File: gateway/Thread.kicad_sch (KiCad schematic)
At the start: 27 parts, among them IC1004 MIC5317-3.3xM5, IC1501 TXB0104RUT, M1501 BT40, Q1501 BSS123, X1501 DEBUG

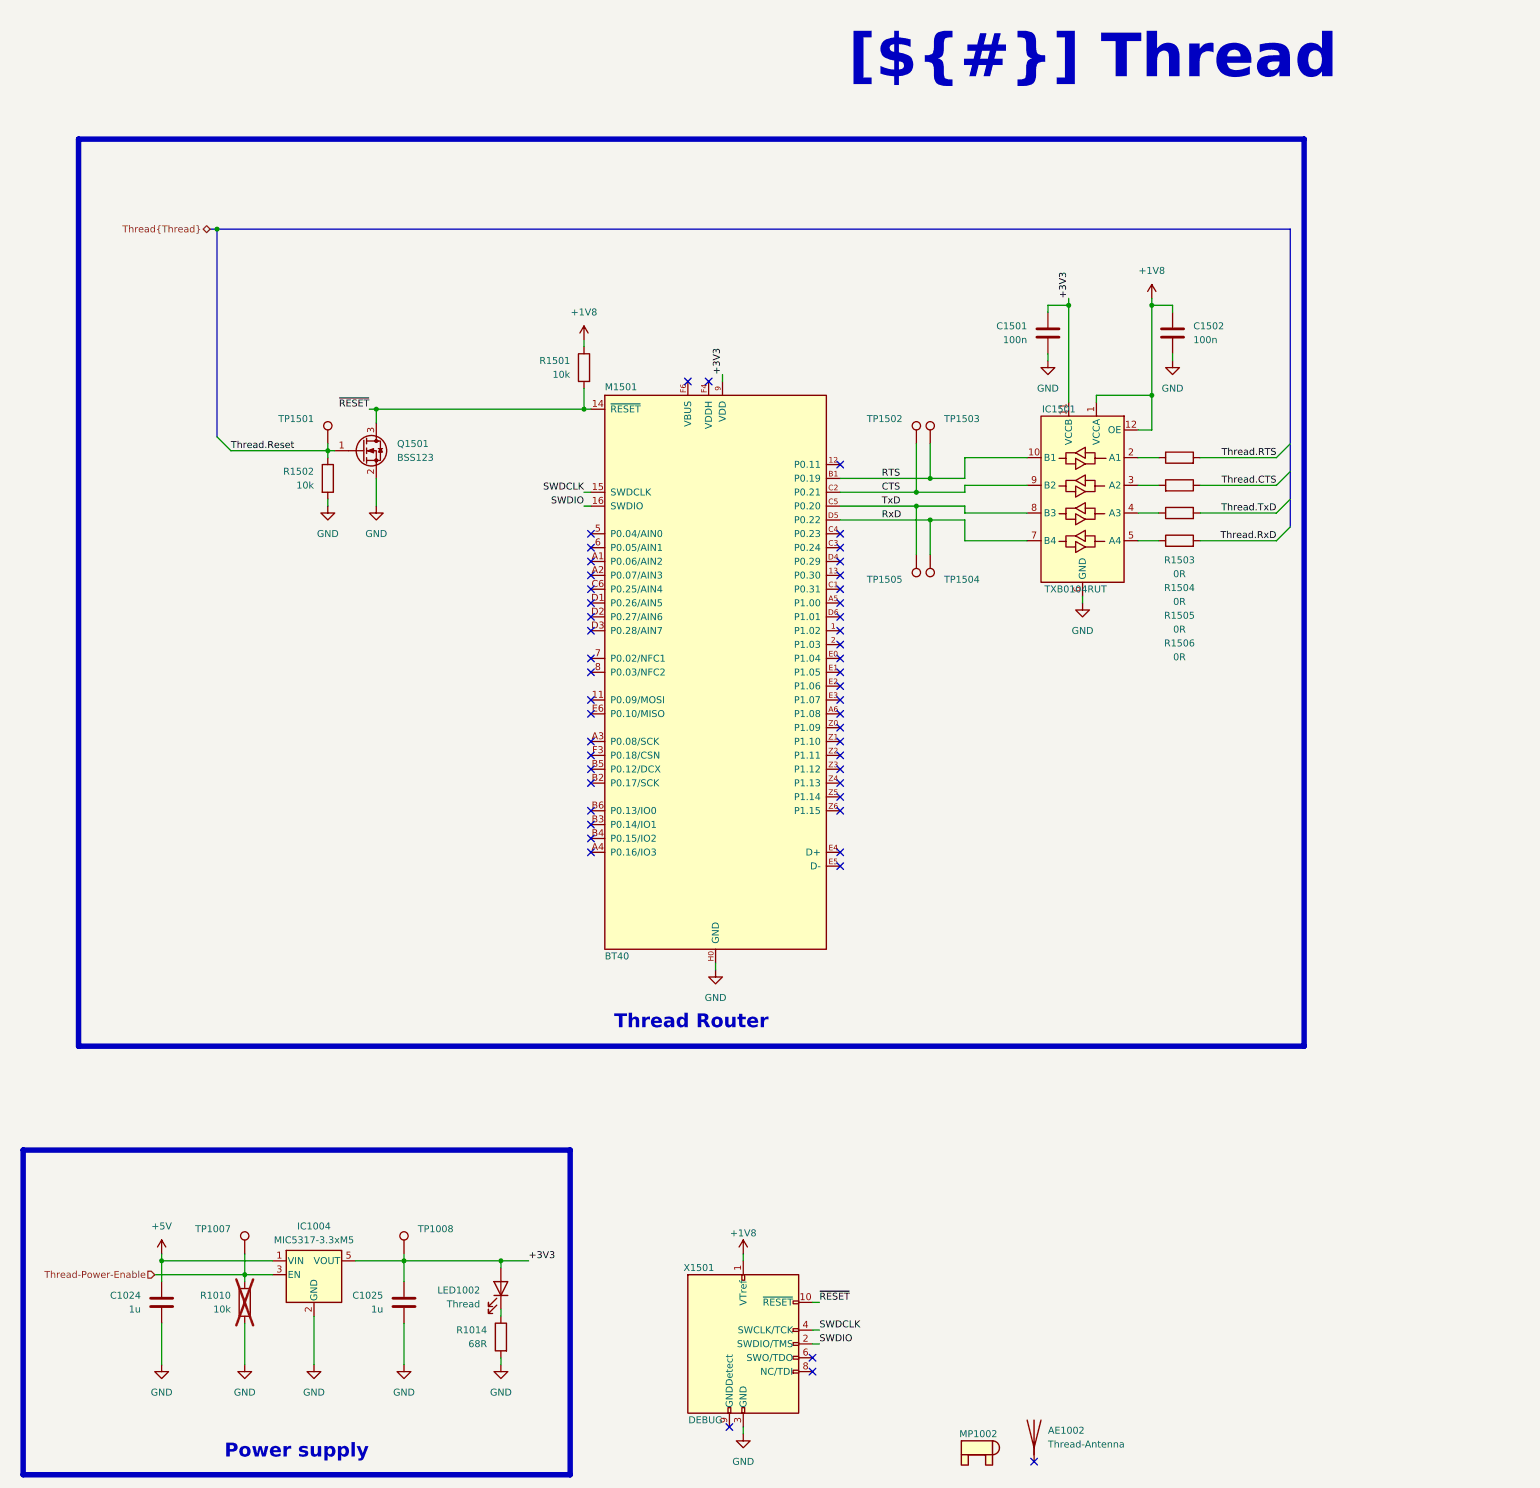
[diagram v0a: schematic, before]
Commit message: Update pin mappings
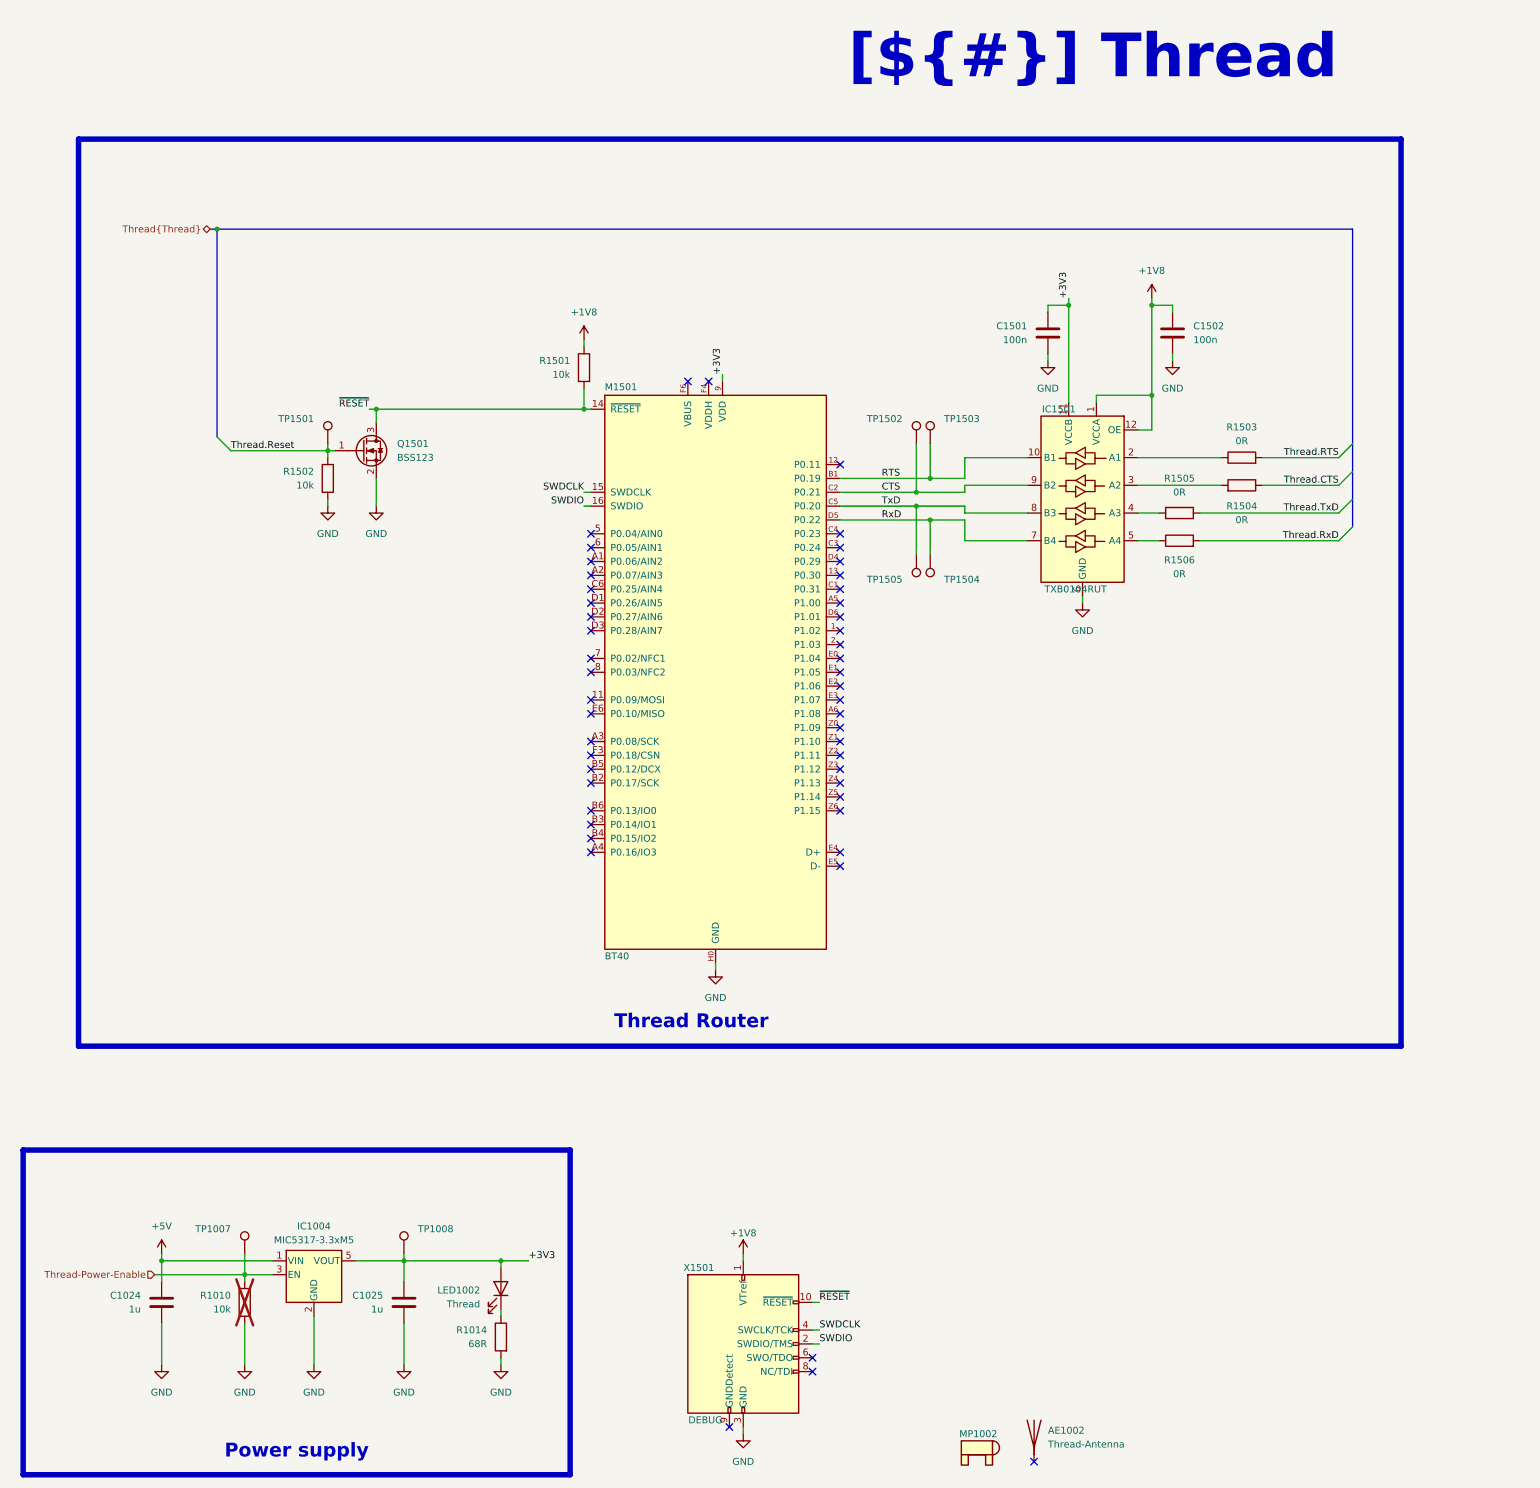
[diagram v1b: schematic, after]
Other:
- moved on the sheet: R1503, R1504
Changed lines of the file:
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@@
 	(rectangle
 		(start 24.13 38.1)
-		(end 248.92 204.47)
+		(end 266.7 204.47)
 		(stroke
 			(width 1)
@@
 	)
 	(junction
-		(at 49.53 54.61)
+		(at 54.61 246.38)
 		(diameter 0)
 		(color 0 0 0 0)
 	)
 	(junction
-		(at 54.61 246.38)
+		(at 177.8 105.41)
 		(diameter 0)
 		(color 0 0 0 0)
 	)
 	(junction
-		(at 177.8 105.41)
+		(at 49.53 54.61)
 		(diameter 0)
 		(color 0 0 0 0)
@@
 	)
 	(bus_entry
-		(at 246.38 93.98)
+		(at 257.81 93.98)
 		(size -2.54 2.54)
 		(stroke
@@
 	)
 	(bus_entry
-		(at 246.38 104.14)
+		(at 257.81 104.14)
 		(size -2.54 2.54)
 		(stroke
@@
 	)
 	(bus_entry
-		(at 246.38 109.22)
+		(at 257.81 109.22)
 		(size -2.54 2.54)
 		(stroke
@@
 	)
 	(bus_entry
-		(at 246.38 99.06)
+		(at 257.81 99.06)
 		(size -2.54 2.54)
 		(stroke
@@
 	(wire
 		(pts
-			(xy 218.44 101.6) (xy 222.25 101.6)
-		)
-		(stroke
-			(width 0)
-			(type default)
-		)
-	)
-	(wire
-		(pts
 			(xy 77.47 87.63) (xy 78.74 87.63)
 		)
@@
 	(wire
 		(pts
-			(xy 229.87 106.68) (xy 243.84 106.68)
+			(xy 229.87 106.68) (xy 255.27 106.68)
 		)
 		(stroke
@@
 	(wire
 		(pts
-			(xy 229.87 101.6) (xy 243.84 101.6)
+			(xy 241.3 101.6) (xy 255.27 101.6)
 		)
 		(stroke
@@
 	(wire
 		(pts
-			(xy 229.87 96.52) (xy 243.84 96.52)
+			(xy 241.3 96.52) (xy 255.27 96.52)
 		)
 		(stroke
@@
 	(bus
 		(pts
-			(xy 246.38 54.61) (xy 246.38 109.22)
+			(xy 257.81 54.61) (xy 257.81 109.22)
 		)
 		(stroke
@@
 	(wire
 		(pts
+			(xy 218.44 101.6) (xy 233.68 101.6)
+		)
+		(stroke
+			(width 0)
+			(type default)
+		)
+	)
+	(wire
+		(pts
 			(xy 142.24 81.28) (xy 142.24 82.55)
 		)
@@
 	(wire
 		(pts
-			(xy 229.87 111.76) (xy 243.84 111.76)
+			(xy 229.87 111.76) (xy 255.27 111.76)
 		)
 		(stroke
@@
 		)
 	)
-	(bus
+	(wire
 		(pts
-			(xy 49.53 54.61) (xy 246.38 54.61)
+			(xy 218.44 96.52) (xy 233.68 96.52)
 		)
 		(stroke
@@
 		)
 	)
-	(wire
+	(bus
 		(pts
-			(xy 101.6 243.84) (xy 106.68 243.84)
+			(xy 49.53 54.61) (xy 257.81 54.61)
 		)
 		(stroke
@@
 	(wire
 		(pts
-			(xy 208.28 121.92) (xy 208.28 123.19)
+			(xy 101.6 243.84) (xy 106.68 243.84)
 		)
 		(stroke
@@
 	(wire
 		(pts
-			(xy 218.44 96.52) (xy 222.25 96.52)
+			(xy 208.28 121.92) (xy 208.28 123.19)
 		)
 		(stroke
@@
 	)
 	(label "Thread.RxD"
-		(at 243.84 111.76 180)
+		(at 255.27 111.76 180)
 		(effects
 			(font
@@
 	)
 	(label "Thread.RTS"
-		(at 243.84 96.52 180)
+		(at 255.27 96.52 180)
 		(effects
 			(font
@@
 	)
 	(label "Thread.TxD"
-		(at 243.84 106.68 180)
+		(at 255.27 106.68 180)
 		(effects
 			(font
@@
 	)
 	(label "Thread.CTS"
-		(at 243.84 101.6 180)
+		(at 255.27 101.6 180)
 		(effects
 			(font
@@
 		(dnp no)
 		(property "Reference" "R1506"
-			(at 226.06 130.556 90)
+			(at 226.06 115.316 90)
 			(show_name no)
 			(do_not_autoplace no)
@@
 		)
 		(property "Value" "0R"
-			(at 226.06 133.096 90)
+			(at 226.06 117.856 90)
 			(show_name no)
 			(do_not_autoplace no)
@@
 	(symbol
 		(lib_id "Device:R")
-		(at 226.06 101.6 270)
+		(at 237.49 101.6 270)
 		(mirror x)
 		(unit 1)
@@
 		(dnp no)
 		(property "Reference" "R1504"
-			(at 226.06 120.396 90)
+			(at 237.49 105.41 90)
 			(show_name no)
 			(do_not_autoplace no)
@@
 		)
 		(property "Value" "0R"
-			(at 226.06 122.936 90)
+			(at 237.49 107.95 90)
 			(show_name no)
 			(do_not_autoplace no)
@@
 		)
 		(property "Footprint" "Resistor_SMD:R_0805_2012Metric"
-			(at 226.06 103.378 90)
+			(at 237.49 103.378 90)
 			(hide yes)
 			(show_name no)
@@
 		)
 		(property "Datasheet" "https://www.mouser.de/datasheet/3/40/1/cr.pdf"
-			(at 226.06 101.6 0)
+			(at 237.49 101.6 0)
 			(hide yes)
 			(show_name no)
@@
 		)
 		(property "Description" "Resistor"
-			(at 226.06 101.6 0)
+			(at 237.49 101.6 0)
 			(hide yes)
 			(show_name no)
@@
 		)
 		(property "manf" "Bourns"
-			(at 226.06 101.6 0)
+			(at 237.49 101.6 0)
 			(hide yes)
 			(show_name no)
@@
 		)
 		(property "manf#" "CR0805-J/-000ELF"
-			(at 226.06 101.6 0)
+			(at 237.49 101.6 0)
 			(hide yes)
 			(show_name no)
@@
 		)
 		(property "mouser#" "652-CR0805-J/-000ELF"
-			(at 226.06 101.6 0)
+			(at 237.49 101.6 0)
 			(hide yes)
 			(show_name no)
@@
 		(in_pos_files yes)
 		(dnp no)
+		(fields_autoplaced yes)
 		(property "Reference" "R1505"
-			(at 226.06 125.476 90)
+			(at 226.06 100.33 90)
 			(show_name no)
 			(do_not_autoplace no)
@@
 		)
 		(property "Value" "0R"
-			(at 226.06 128.016 90)
+			(at 226.06 102.87 90)
 			(show_name no)
 			(do_not_autoplace no)
@@
 	(symbol
 		(lib_id "Device:R")
-		(at 226.06 96.52 90)
+		(at 237.49 96.52 90)
 		(unit 1)
 		(body_style 1)
@@
 		(dnp no)
 		(property "Reference" "R1503"
-			(at 226.06 115.316 90)
+			(at 237.49 90.932 90)
 			(show_name no)
 			(do_not_autoplace no)
@@
 		)
 		(property "Value" "0R"
-			(at 226.06 117.856 90)
+			(at 237.49 93.472 90)
 			(show_name no)
 			(do_not_autoplace no)
@@
 		)
 		(property "Footprint" "Resistor_SMD:R_0805_2012Metric"
-			(at 226.06 98.298 90)
+			(at 237.49 98.298 90)
 			(hide yes)
 			(show_name no)
@@
 		)
 		(property "Datasheet" "https://www.mouser.de/datasheet/3/40/1/cr.pdf"
-			(at 226.06 96.52 0)
+			(at 237.49 96.52 0)
 			(hide yes)
 			(show_name no)
@@
 		)
 		(property "Description" "Resistor"
-			(at 226.06 96.52 0)
+			(at 237.49 96.52 0)
 			(hide yes)
 			(show_name no)
@@
 		)
 		(property "manf" "Bourns"
-			(at 226.06 96.52 0)
+			(at 237.49 96.52 0)
 			(hide yes)
 			(show_name no)
@@
 		)
 		(property "manf#" "CR0805-J/-000ELF"
-			(at 226.06 96.52 0)
+			(at 237.49 96.52 0)
 			(hide yes)
 			(show_name no)
@@
 		)
 		(property "mouser#" "652-CR0805-J/-000ELF"
-			(at 226.06 96.52 0)
+			(at 237.49 96.52 0)
 			(hide yes)
 			(show_name no)

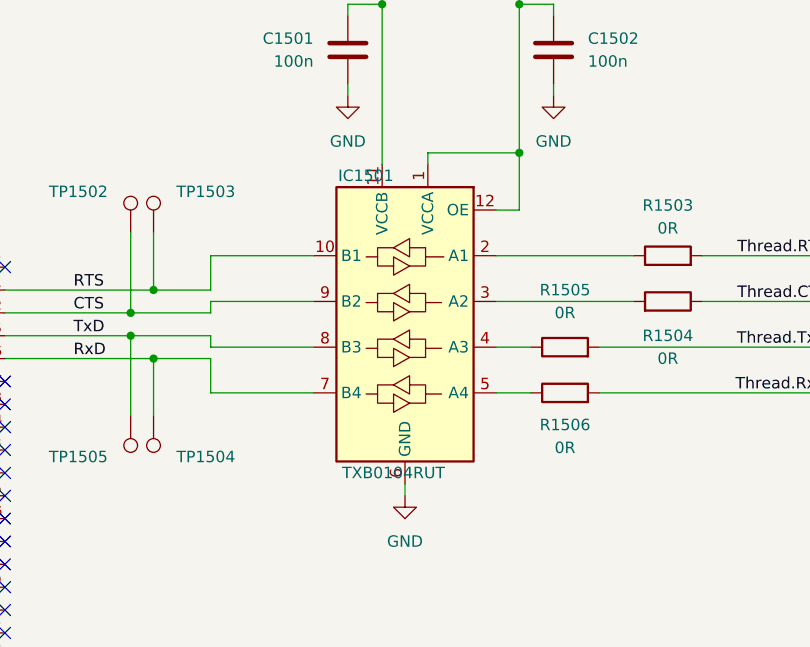
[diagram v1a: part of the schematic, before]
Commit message: Adding level shifter, update documentation
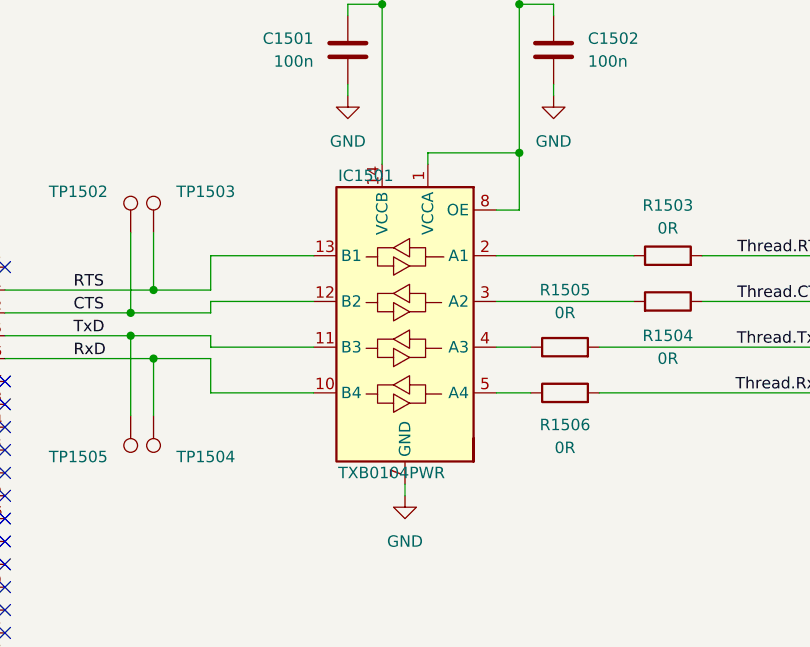
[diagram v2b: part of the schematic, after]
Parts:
- IC1501: value TXB0104RUT -> TXB0104PWR; footprint Package_DFN_QFN:Texas_R-PUQFN-N12 -> Package_SO:TSSOP-14_4.4x5mm_P0.65mm; symbol Logic_LevelTranslator:TXB0104RUT -> Logic_LevelTranslator:TXB0104PW; manf# TXB0104RUTR -> TXB0104PWR; mouser# 595-TXB0104RUTR -> 595-TXB0104PWR
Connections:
- net +1V8: now also IC1501.8 (OE); no longer IC1501.12 (OE)
- net +3V3: now also IC1501.14 (VCCB); no longer IC1501.11 (VCCB)
- net CTS: now also IC1501.12 (B2); no longer IC1501.9 (B2)
- net GND: now also IC1501.7 (GND); no longer IC1501.6 (GND)
- net RTS: now also IC1501.13 (B1); no longer IC1501.10 (B1)
- net RxD: now also IC1501.10 (B4); no longer IC1501.7 (B4)
- net TxD: now also IC1501.11 (B3); no longer IC1501.8 (B3)
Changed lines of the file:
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@@
 	)
 	(symbol
-		(lib_id "Logic_LevelTranslator:TXB0104RUT")
+		(lib_id "Logic_LevelTranslator:TXB0104PW")
 		(at 208.28 104.14 0)
 		(mirror y)
@@
 			)
 		)
-		(property "Value" "TXB0104RUT"
+		(property "Value" "TXB0104PWR"
 			(at 212.725 120.65 0)
 			(show_name no)
@@
 			)
 		)
-		(property "Footprint" "Package_DFN_QFN:Texas_R-PUQFN-N12"
+		(property "Footprint" "Package_SO:TSSOP-14_4.4x5mm_P0.65mm"
 			(at 208.28 123.19 0)
 			(hide yes)
@@
 			)
 		)
-		(property "Description" "4-Bit Bidirectional Voltage-Level Translator, Auto Direction Sensing and ±15-kV ESD Protection, 1.2 - 3.6V APort, 1.65 - 5.5V BPort, Texas_PUQFN-12"
+		(property "Description" "4-Bit Bidirectional Voltage-Level Translator, Auto Direction Sensing and ±15-kV ESD Protection, 1.2 - 3.6V APort, 1.65 - 5.5V BPort, TSSOP-14"
 			(at 208.28 104.14 0)
 			(hide yes)
@@
 			)
 		)
-		(property "manf#" "TXB0104RUTR"
+		(property "manf#" "TXB0104PWR"
 			(at 208.28 104.14 0)
 			(hide yes)
@@
 			)
 		)
-		(property "mouser#" "595-TXB0104RUTR"
+		(property "mouser#" "595-TXB0104PWR"
 			(at 208.28 104.14 0)
 			(hide yes)
@@
 		(pin "8"
 		)
+		(pin "13"
+		)
+		(pin "14"
+		)
 		(instances
